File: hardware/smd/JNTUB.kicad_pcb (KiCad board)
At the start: 2 copper layers, 41.1 x 110.7 mm, 86 parts, among them J1 3.5mm Mono Jack, J10 B2_HDR, J11 B2_HDR, J12 ISP, J2 3.5mm Mono Jack, J3 3.5mm Mono Jack, J4 3.5mm Mono Jack, J5 3.5mm Mono Jack, J6 3.5mm Mono Jack, J7 B1_HDR, J8 B1_HDR, J9 POWER_HDR, Q1 MMBT3904, Q2 MMBT3904, Q3 MMBT3904, U1 ATtiny85, U2 TL074, U3 78L05, U4 79L05

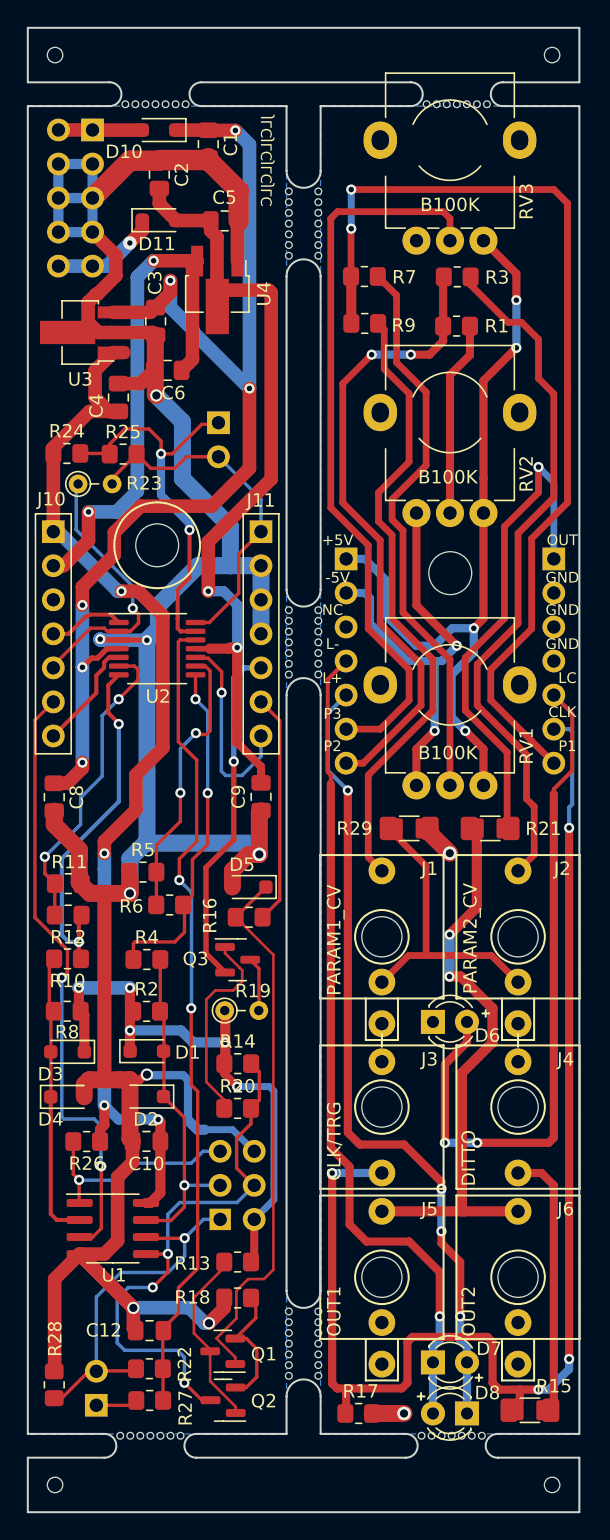
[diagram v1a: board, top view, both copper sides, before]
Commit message: Made control board all through-hole.
Reasoning: For JLC production it usually ends up cheaper to not provide user panelized boards with "two designs". By making only one board SMD, we can de-panelize and only do PCBA on the main board - this is about 20% cheaper (for 10 pairs of boards). The tradeoff is we have to solder 8 extra THT resistors.
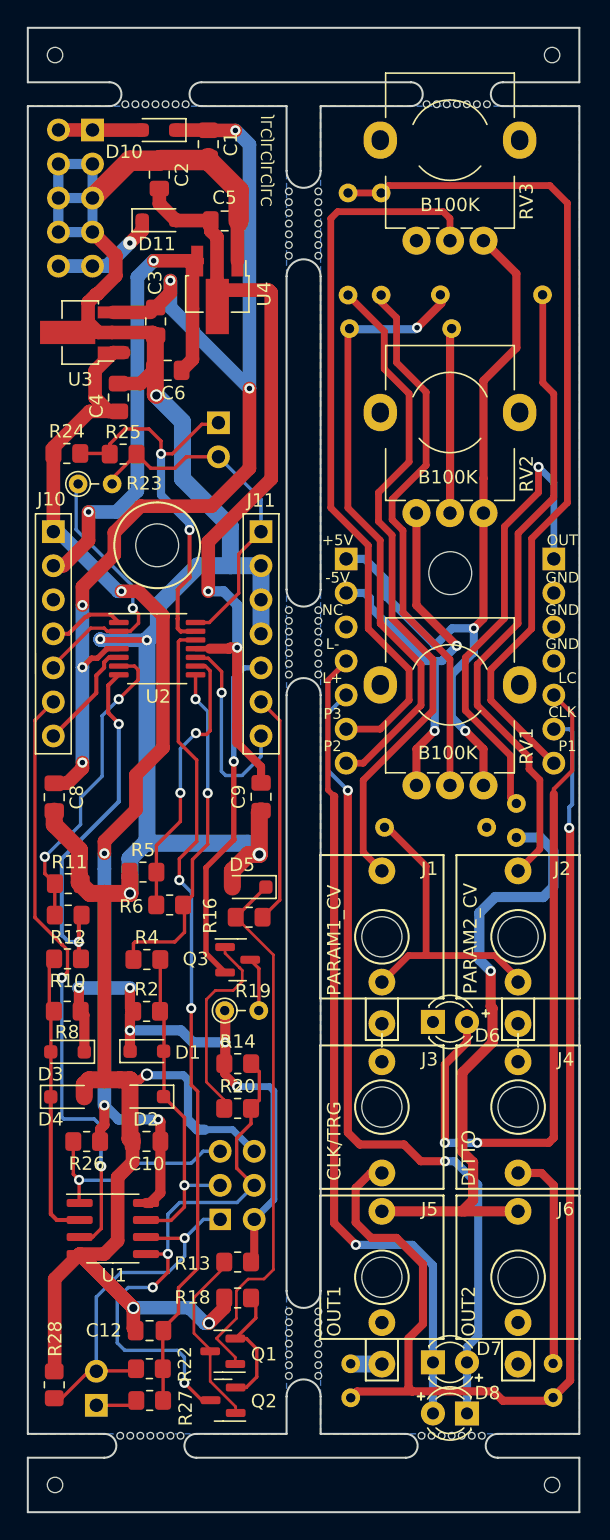
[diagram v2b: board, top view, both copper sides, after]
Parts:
- C12: value 1.8n -> 2.2n
- R1, R3, R7, R9: footprint Resistor_SMD:R_0805_2012Metric_Pad1.20x1.40mm_HandSolder -> Resistor_THT:R_Axial_DIN0204_L3.6mm_D1.6mm_P7.62mm_Horizontal; moved to B.Cu
- R15, R21: footprint SMD:R_1206-0805_combo -> Resistor_THT:R_Axial_DIN0204_L3.6mm_D1.6mm_P2.54mm_Vertical; moved to B.Cu
- R17: footprint Resistor_SMD:R_0805_2012Metric_Pad1.20x1.40mm_HandSolder -> Resistor_THT:R_Axial_DIN0204_L3.6mm_D1.6mm_P2.54mm_Vertical; moved to B.Cu
- R29: footprint SMD:R_1206-0805_combo -> Resistor_THT:R_Axial_DIN0204_L3.6mm_D1.6mm_P7.62mm_Horizontal; moved to B.Cu
- moved R1 7.99 mm to (220.1, 74.5)
- moved R29 5.78 mm to (230.3, 111.7)
- moved R17 3.76 mm to (220.2, 151.7), turned to -90 degrees
- moved R9 2.45 mm to (220.0, 72.0), turned to 90 degrees
- moved R21 2.07 mm to (232.5, 112.5), turned to 90 degrees
- moved R15 1.97 mm to (235.3, 154.3), turned to 90 degrees
- moved R7 1.87 mm to (222.4, 72.0), turned to 90 degrees
- moved R3 1.84 mm to (226.9, 72.0)
- gave numbers to parts that had none: 2
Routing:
- net /PeripheralBoard/P1_AVG: track 72.7 -> 63.2 mm, vias 2 -> 0
- net /PeripheralBoard/CLK_TRG: track 97.5 -> 88.8 mm, vias 4 -> 1
- net /PeripheralBoard/OUT1: track 42.6 -> 46.6 mm, vias 2 -> 1
- net /PeripheralBoard/P2_CV: track 52.1 -> 48.3 mm
- net /PeripheralBoard/DITTO: track 19.9 -> 16.4 mm
- net /PeripheralBoard/P1_CV: track 46.9 -> 50.2 mm
- net GNDREF: track 227.8 -> 225.3 mm, vias 10 -> 8
- net /PeripheralBoard/OUT: track 38.0 -> 36.3 mm
- net /PeripheralBoard/LED_POS: track 60.9 -> 62.6 mm, vias 4 -> 2
- net /PeripheralBoard/P1_POT: track 42.3 -> 40.8 mm
- net /PeripheralBoard/P2_AVG: track 47.4 -> 46.1 mm, vias 2 -> 1
- net +5V: track 185.4 -> 184.6 mm, vias 13 -> 11
- net /PeripheralBoard/P2_POT: track 14.6 -> 13.8 mm
- net -5V: track 72.5 -> 71.7 mm

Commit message: Depanelize SMD PCBs.
It typically turns out cheaper to NOT panelize for smaller JLC runs. Also means no  residual mousebite overhangs that might need sanding back.
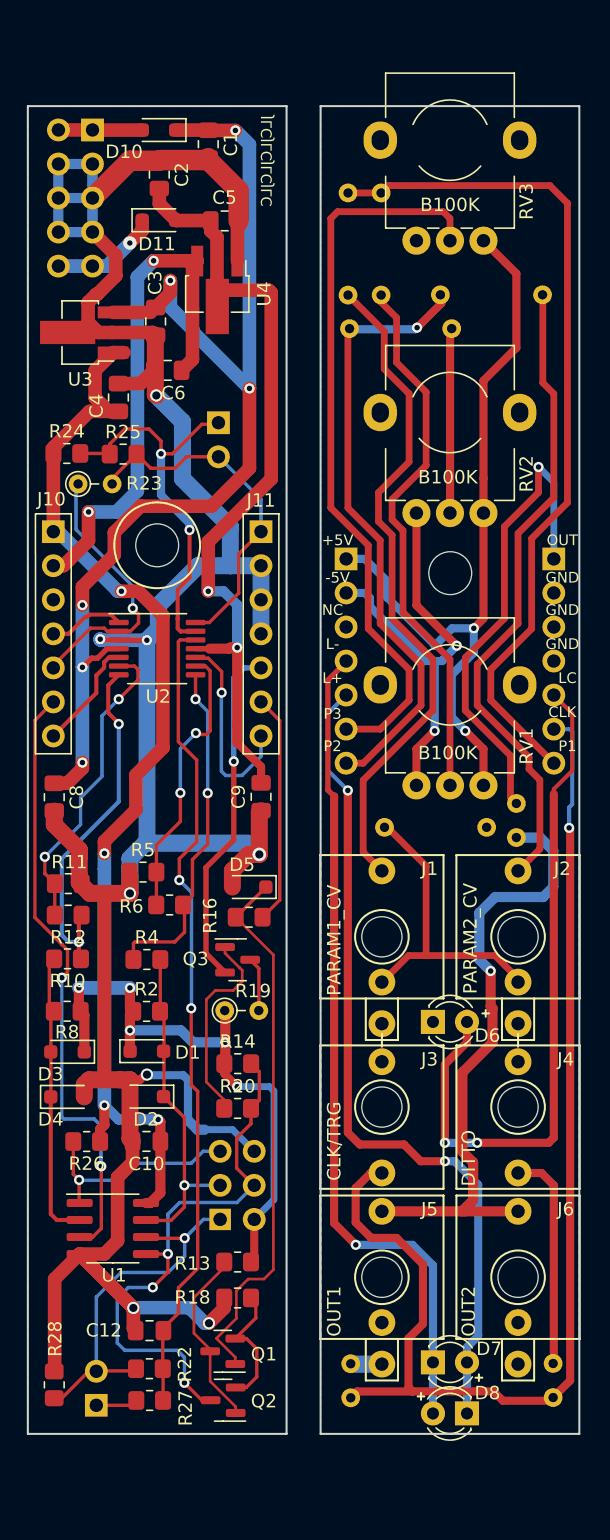
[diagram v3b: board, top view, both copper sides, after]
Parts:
- removed ? (x3): , Panelization:mouse-bite-2.54mm-slot-long
- removed ? (x4): Hole_Tooling, SDIY:Hole_Tooling
- removed ? (x4): , Panelization:mouse-bite-2mm-slot-long-single
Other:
- board size 41.1 x 110.7 mm -> 41.1 x 99.1 mm

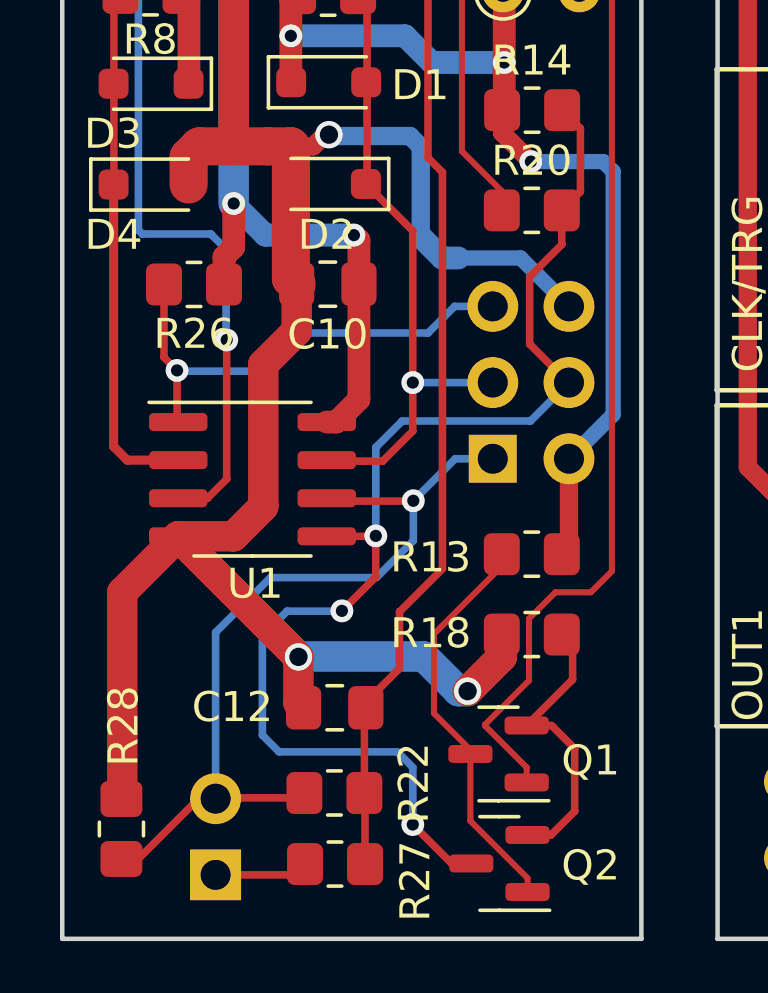
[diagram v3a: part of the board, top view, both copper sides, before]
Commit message: Fix footprint for ATtiny85 (wide SOIC-8).
Add "JLCPCB Rotation Offset" field with rotations for U and Q components.
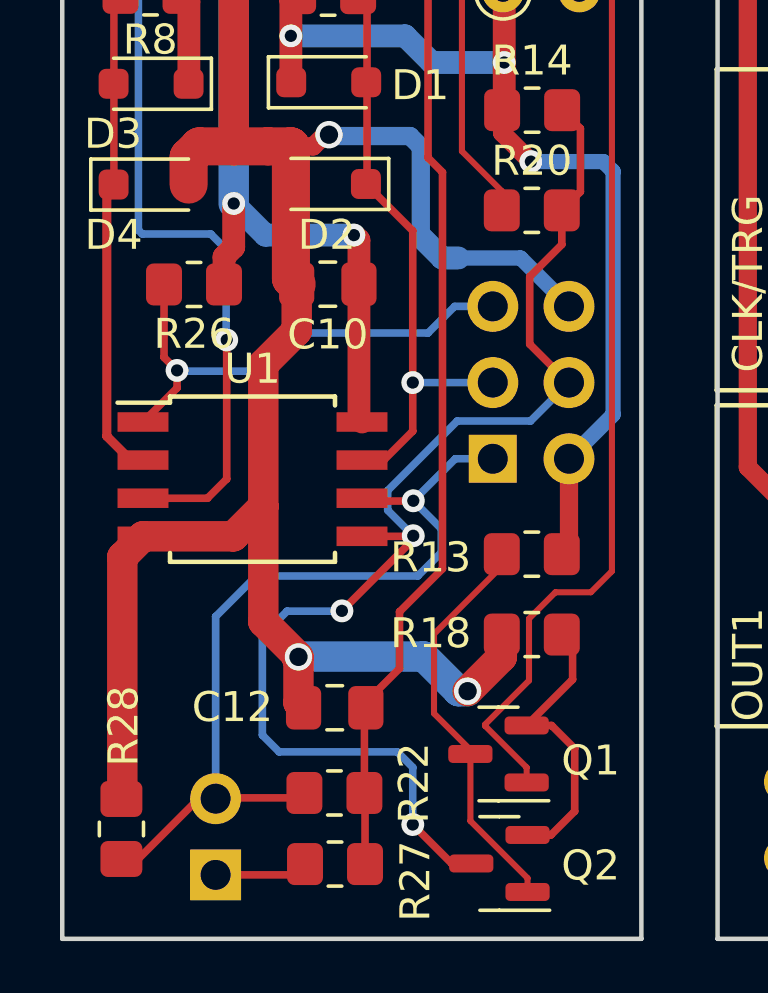
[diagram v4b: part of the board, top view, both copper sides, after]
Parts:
- U1: footprint Package_SO:SOIC-8_3.9x4.9mm_P1.27mm -> Package_SO:SOIC-8W_5.3x5.3mm_P1.27mm
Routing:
- net GNDREF: track 225.3 -> 220.3 mm
- net /MainBoard/MCU_ADC1: track 25.2 -> 24.0 mm
- net /MainBoard/MCU_ADC2: track 45.5 -> 46.7 mm
- net /MainBoard/MCU_ADC3: track 21.8 -> 20.7 mm
- net /MainBoard/MCU_PWM: track 27.9 -> 28.6 mm
- net +5V: track 184.6 -> 184.0 mm
